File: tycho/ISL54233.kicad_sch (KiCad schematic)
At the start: 4 parts, among them U17 ISL54233

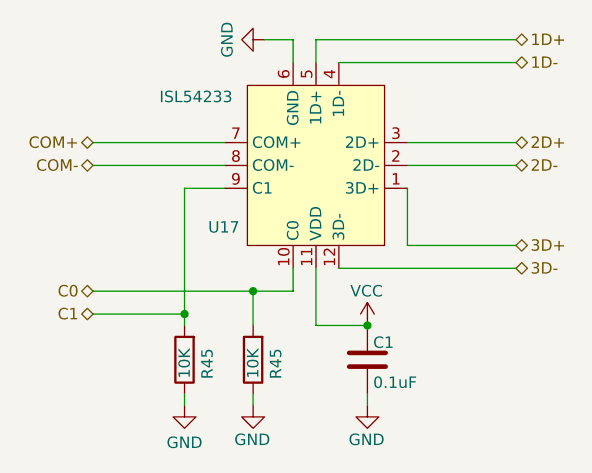
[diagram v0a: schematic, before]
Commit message: ERC cleanup put everything on 0.05mm grid
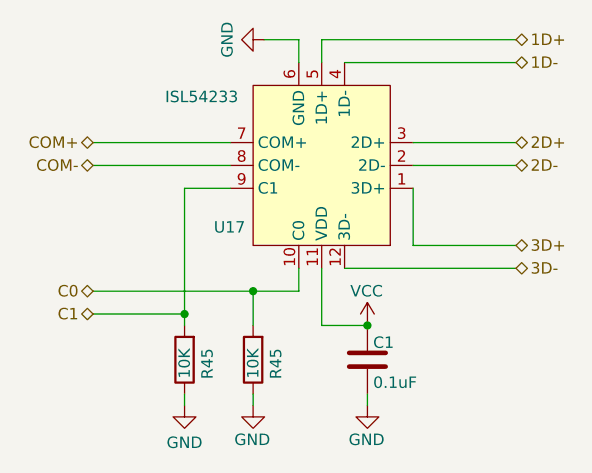
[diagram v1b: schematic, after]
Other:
- moved on the sheet: U17
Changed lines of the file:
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@@
     (stroke (width 0) (type default))
   )
-  (wire (pts (xy 163.195 99.06) (xy 163.195 92.71))
+  (wire (pts (xy 163.83 99.06) (xy 163.83 92.71))
     (stroke (width 0) (type default))
   )
@@
     (stroke (width 0) (type default))
   )
-  (wire (pts (xy 153.035 101.6) (xy 153.035 107.95))
-    (stroke (width 0) (type default))
-  )
-  (wire (pts (xy 150.495 76.2) (xy 147.32 76.2))
-    (stroke (width 0) (type default))
-  )
-  (wire (pts (xy 153.035 76.2) (xy 153.035 78.74))
-    (stroke (width 0) (type default))
-  )
-  (wire (pts (xy 175.26 87.63) (xy 163.195 87.63))
-    (stroke (width 0) (type default))
-  )
-  (wire (pts (xy 175.26 78.74) (xy 155.575 78.74))
-    (stroke (width 0) (type default))
-  )
-  (wire (pts (xy 128.27 90.17) (xy 142.875 90.17))
+  (wire (pts (xy 153.67 101.6) (xy 153.67 107.95))
+    (stroke (width 0) (type default))
+  )
+  (wire (pts (xy 151.13 76.2) (xy 147.32 76.2))
+    (stroke (width 0) (type default))
+  )
+  (wire (pts (xy 153.67 76.2) (xy 153.67 78.74))
+    (stroke (width 0) (type default))
+  )
+  (wire (pts (xy 175.26 87.63) (xy 163.83 87.63))
+    (stroke (width 0) (type default))
+  )
+  (wire (pts (xy 175.26 78.74) (xy 156.21 78.74))
+    (stroke (width 0) (type default))
+  )
+  (wire (pts (xy 128.27 90.17) (xy 143.51 90.17))
     (stroke (width 0) (type default))
   )
@@
     (stroke (width 0) (type default))
   )
-  (wire (pts (xy 175.26 76.2) (xy 153.035 76.2))
-    (stroke (width 0) (type default))
-  )
-  (wire (pts (xy 155.575 101.6) (xy 175.26 101.6))
-    (stroke (width 0) (type default))
-  )
-  (wire (pts (xy 146.05 104.14) (xy 150.495 104.14))
-    (stroke (width 0) (type default))
-  )
-  (wire (pts (xy 138.43 92.71) (xy 142.875 92.71))
-    (stroke (width 0) (type default))
-  )
-  (wire (pts (xy 175.26 99.06) (xy 163.195 99.06))
+  (wire (pts (xy 175.26 76.2) (xy 153.67 76.2))
+    (stroke (width 0) (type default))
+  )
+  (wire (pts (xy 156.21 101.6) (xy 175.26 101.6))
+    (stroke (width 0) (type default))
+  )
+  (wire (pts (xy 146.05 104.14) (xy 151.13 104.14))
+    (stroke (width 0) (type default))
+  )
+  (wire (pts (xy 138.43 92.71) (xy 143.51 92.71))
+    (stroke (width 0) (type default))
+  )
+  (wire (pts (xy 175.26 99.06) (xy 163.83 99.06))
     (stroke (width 0) (type default))
   )
@@
     (stroke (width 0) (type default))
   )
-  (wire (pts (xy 153.035 107.95) (xy 158.75 107.95))
-    (stroke (width 0) (type default))
-  )
-  (wire (pts (xy 175.26 90.17) (xy 163.195 90.17))
-    (stroke (width 0) (type default))
-  )
-  (wire (pts (xy 128.27 87.63) (xy 142.875 87.63))
-    (stroke (width 0) (type default))
-  )
-  (wire (pts (xy 150.495 104.14) (xy 150.495 101.6))
+  (wire (pts (xy 153.67 107.95) (xy 158.75 107.95))
+    (stroke (width 0) (type default))
+  )
+  (wire (pts (xy 175.26 90.17) (xy 163.83 90.17))
+    (stroke (width 0) (type default))
+  )
+  (wire (pts (xy 128.27 87.63) (xy 143.51 87.63))
+    (stroke (width 0) (type default))
+  )
+  (wire (pts (xy 151.13 104.14) (xy 151.13 101.6))
     (stroke (width 0) (type default))
   )
@@
     (stroke (width 0) (type default))
   )
-  (wire (pts (xy 150.495 76.2) (xy 150.495 78.74))
+  (wire (pts (xy 151.13 76.2) (xy 151.13 78.74))
     (stroke (width 0) (type default))
   )
@@
     )
   )
-  (symbol (lib_id "tycho:ISL54233") (at 153.035 90.17 180) (unit 1)
+  (symbol (lib_id "tycho:ISL54233") (at 153.67 90.17 180) (unit 1)
     (in_bom yes) (on_board yes) (dnp no)
-    (property "Reference" "U17" (at 142.7941 97.0402 0)
-      (effects (font (size 1.27 1.27)))
-    )
-    (property "Value" "ISL54233" (at 139.7 82.55 0)
-      (effects (font (size 1.27 1.27)))
-    )
-    (property "Footprint" "Package_DFN_QFN:QFN-12-1EP_3x3mm_P0.51mm_EP1.45x1.45mm" (at 153.035 90.17 0)
-      (effects (font (size 1.27 1.27)) hide)
-    )
-    (property "Datasheet" "https://www.renesas.com/us/en/document/dst/isl54233-datasheet" (at 153.035 90.17 0)
-      (effects (font (size 1.27 1.27)) hide)
-    )
-    (property "Manufacturer" "Renesas Electronics America Inc" (at 153.035 90.17 0)
-      (effects (font (size 1.27 1.27)) hide)
-    )
-    (property "Part Number" "ISL54233IRTZ-T" (at 153.035 90.17 0)
-      (effects (font (size 1.27 1.27)) hide)
-    )
-    (property "Description" "IC SWITCH SP3T X 2 15OHM 12TQFN" (at 153.035 90.17 0)
-      (effects (font (size 1.27 1.27)) hide)
-    )
+    (property "Reference" "U17" (at 143.4291 97.0402 0)
+      (effects (font (size 1.27 1.27)))
+    )
+    (property "Value" "ISL54233" (at 140.335 82.55 0)
+      (effects (font (size 1.27 1.27)))
+    )
+    (property "Footprint" "Package_DFN_QFN:QFN-12-1EP_3x3mm_P0.51mm_EP1.45x1.45mm" (at 153.67 90.17 0)
+      (effects (font (size 1.27 1.27)) hide)
+    )
+    (property "Datasheet" "https://www.renesas.com/us/en/document/dst/isl54233-datasheet" (at 153.67 90.17 0)
+      (effects (font (size 1.27 1.27)) hide)
+    )
+    (property "Manufacturer" "Renesas Electronics America Inc" (at 153.67 90.17 0)
+      (effects (font (size 1.27 1.27)) hide)
+    )
+    (property "Part Number" "ISL54233IRTZ-T" (at 153.67 90.17 0)
+      (effects (font (size 1.27 1.27)) hide)
+    )
+    (property "Description" "IC SWITCH SP3T X 2 15OHM 12TQFN" (at 153.67 90.17 0)
+      (effects (font (size 1.27 1.27)) hide)
+    )

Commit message: Update part numbers
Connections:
- net GND: now also U17.13 (GND)
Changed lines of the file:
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@@
     (pin "8")
     (pin "9")
+    (pin "13")
     (instances
       (project "tycho"

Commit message: Update revision number, metadata, and schematic page numbers
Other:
- company: (none) -> Copyright 2023 Great Scott Gadgets
- title: (none) -> Tycho
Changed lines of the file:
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@@
 (kicad_sch (version 20230121) (generator eeschema)
   (paper "A4")
+  (title_block
+    (title "Tycho")
+    (date "${DATE}")
+    (rev "${VERSION}")
+    (company "Copyright 2023 Great Scott Gadgets")
+    (comment 1 "Licensed under the CERN-OHL-P v2")
+  )
   (junction (at 158.75 107.95) (diameter 0) (color 0 0 0 0)
   )

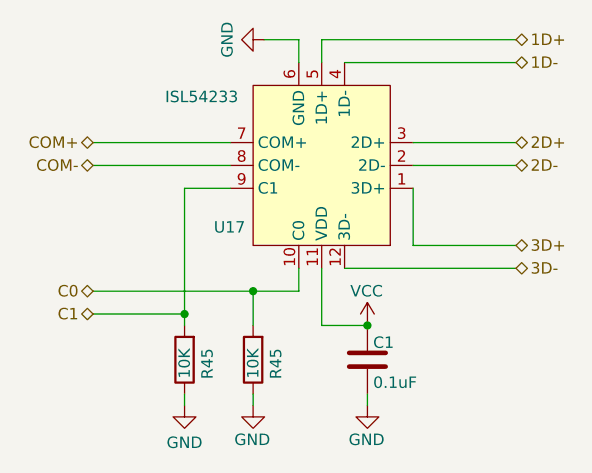
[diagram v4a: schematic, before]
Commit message: Change R65 to 22k
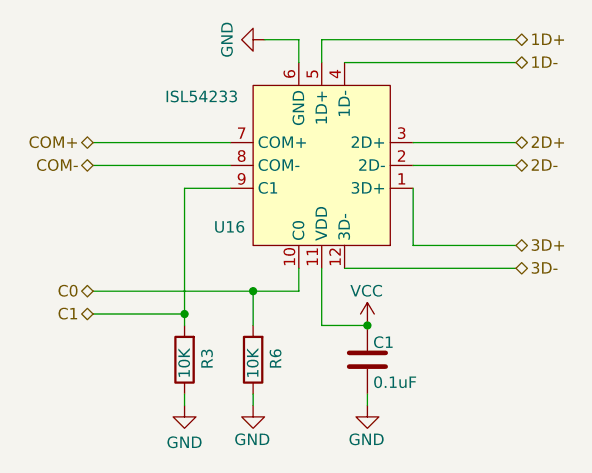
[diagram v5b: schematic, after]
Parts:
- renumbered R45 to R3, R45 to R6, U17 to U16
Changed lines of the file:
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@@
   (symbol (lib_id "power:GND") (at 147.32 76.2 270) (unit 1)
     (in_bom yes) (on_board yes) (dnp no) (fields_autoplaced)
-    (property "Reference" "#PWR077" (at 140.97 76.2 0)
+    (property "Reference" "#PWR05" (at 140.97 76.2 0)
       (effects (font (size 1.27 1.27)) hide)
     )
@@
     (instances
       (project "tycho"
-        (path "/4ed1cbaf-15e8-40e5-8366-86487d525fd5"
-          (reference "#PWR077") (unit 1)
-        )
         (path "/4ed1cbaf-15e8-40e5-8366-86487d525fd5/63918e02-2e47-48d0-bbb9-fd752ccc3b47"
           (reference "#PWR05") (unit 1)
@@
   (symbol (lib_id "Device:R") (at 146.05 111.76 180) (unit 1)
     (in_bom yes) (on_board yes) (dnp no)
-    (property "Reference" "R45" (at 148.59 110.49 90)
+    (property "Reference" "R6" (at 148.59 110.49 90)
       (effects (font (size 1.27 1.27)) (justify left))
     )
@@
     (instances
       (project "tycho"
-        (path "/4ed1cbaf-15e8-40e5-8366-86487d525fd5/adaa3f42-a370-4a4c-b378-51d1ea5352f8"
-          (reference "R45") (unit 1)
-        )
-        (path "/4ed1cbaf-15e8-40e5-8366-86487d525fd5"
-          (reference "R3") (unit 1)
-        )
         (path "/4ed1cbaf-15e8-40e5-8366-86487d525fd5/63918e02-2e47-48d0-bbb9-fd752ccc3b47"
           (reference "R6") (unit 1)
@@
     (instances
       (project "tycho"
-        (path "/4ed1cbaf-15e8-40e5-8366-86487d525fd5"
+        (path "/4ed1cbaf-15e8-40e5-8366-86487d525fd5/63918e02-2e47-48d0-bbb9-fd752ccc3b47"
           (reference "#PWR06") (unit 1)
         )
-        (path "/4ed1cbaf-15e8-40e5-8366-86487d525fd5/63918e02-2e47-48d0-bbb9-fd752ccc3b47"
-          (reference "#PWR06") (unit 1)
-        )
       )
     )
@@
     (instances
       (project "tycho"
-        (path "/4ed1cbaf-15e8-40e5-8366-86487d525fd5"
+        (path "/4ed1cbaf-15e8-40e5-8366-86487d525fd5/63918e02-2e47-48d0-bbb9-fd752ccc3b47"
           (reference "C1") (unit 1)
         )
-        (path "/4ed1cbaf-15e8-40e5-8366-86487d525fd5/175ec40e-e1eb-4798-86e4-603e661ed6e0"
-          (reference "C24") (unit 1)
-        )
-        (path "/4ed1cbaf-15e8-40e5-8366-86487d525fd5/63918e02-2e47-48d0-bbb9-fd752ccc3b47"
-          (reference "C1") (unit 1)
-        )
       )
     )
@@
   (symbol (lib_id "tycho:ISL54233") (at 153.67 90.17 180) (unit 1)
     (in_bom yes) (on_board yes) (dnp no)
-    (property "Reference" "U17" (at 143.4291 97.0402 0)
+    (property "Reference" "U16" (at 143.4291 97.0402 0)
       (effects (font (size 1.27 1.27)))
     )
@@
     (instances
       (project "tycho"
-        (path "/4ed1cbaf-15e8-40e5-8366-86487d525fd5"
-          (reference "U17") (unit 1)
-        )
         (path "/4ed1cbaf-15e8-40e5-8366-86487d525fd5/63918e02-2e47-48d0-bbb9-fd752ccc3b47"
           (reference "U16") (unit 1)
@@
   (symbol (lib_id "power:GND") (at 158.75 116.84 0) (unit 1)
     (in_bom yes) (on_board yes) (dnp no)
-    (property "Reference" "#PWR05" (at 158.75 123.19 0)
+    (property "Reference" "#PWR07" (at 158.75 123.19 0)
       (effects (font (size 1.27 1.27)) hide)
     )
@@
     (instances
       (project "tycho"
-        (path "/4ed1cbaf-15e8-40e5-8366-86487d525fd5"
-          (reference "#PWR05") (unit 1)
-        )
         (path "/4ed1cbaf-15e8-40e5-8366-86487d525fd5/63918e02-2e47-48d0-bbb9-fd752ccc3b47"
           (reference "#PWR07") (unit 1)
@@
   (symbol (lib_id "power:GND") (at 146.05 116.84 0) (unit 1)
     (in_bom yes) (on_board yes) (dnp no)
-    (property "Reference" "#PWR05" (at 146.05 123.19 0)
+    (property "Reference" "#PWR077" (at 146.05 123.19 0)
       (effects (font (size 1.27 1.27)) hide)
     )
@@
     (instances
       (project "tycho"
-        (path "/4ed1cbaf-15e8-40e5-8366-86487d525fd5"
-          (reference "#PWR05") (unit 1)
-        )
         (path "/4ed1cbaf-15e8-40e5-8366-86487d525fd5/63918e02-2e47-48d0-bbb9-fd752ccc3b47"
           (reference "#PWR077") (unit 1)
@@
   (symbol (lib_id "Device:R") (at 138.43 111.76 180) (unit 1)
     (in_bom yes) (on_board yes) (dnp no)
-    (property "Reference" "R45" (at 140.97 110.49 90)
+    (property "Reference" "R3" (at 140.97 110.49 90)
       (effects (font (size 1.27 1.27)) (justify left))
     )
@@
     (instances
       (project "tycho"
-        (path "/4ed1cbaf-15e8-40e5-8366-86487d525fd5/adaa3f42-a370-4a4c-b378-51d1ea5352f8"
-          (reference "R45") (unit 1)
-        )
-        (path "/4ed1cbaf-15e8-40e5-8366-86487d525fd5"
-          (reference "R6") (unit 1)
-        )
         (path "/4ed1cbaf-15e8-40e5-8366-86487d525fd5/63918e02-2e47-48d0-bbb9-fd752ccc3b47"
           (reference "R3") (unit 1)
@@
   (symbol (lib_id "power:VCC") (at 158.75 107.95 0) (unit 1)
     (in_bom yes) (on_board yes) (dnp no)
-    (property "Reference" "#PWR0116" (at 158.75 111.76 0)
+    (property "Reference" "#PWR08" (at 158.75 111.76 0)
       (effects (font (size 1.27 1.27)) hide)
     )
@@
     (instances
       (project "tycho"
-        (path "/4ed1cbaf-15e8-40e5-8366-86487d525fd5/222b4080-8d34-44ed-a5b0-a264978495bc"
-          (reference "#PWR0116") (unit 1)
-        )
-        (path "/4ed1cbaf-15e8-40e5-8366-86487d525fd5/b101adbb-56d2-408d-a053-b060f8f597ee"
-          (reference "#PWR0120") (unit 1)
-        )
-        (path "/4ed1cbaf-15e8-40e5-8366-86487d525fd5"
-          (reference "#PWR07") (unit 1)
-        )
         (path "/4ed1cbaf-15e8-40e5-8366-86487d525fd5/63918e02-2e47-48d0-bbb9-fd752ccc3b47"
           (reference "#PWR08") (unit 1)
